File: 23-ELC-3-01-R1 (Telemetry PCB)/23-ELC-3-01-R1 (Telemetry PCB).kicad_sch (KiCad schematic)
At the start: 27 parts, among them J1 Conn_01x02, J10 Conn_02x12_Top_Bottom, J104 Raspberry_Pi_4b, J105 Conn_01x01, J106 Fan Header, J2 Conn_01x08, J4 Conn_01x02, J5 Conn_01x02, J7 Conn_01x08, J8 Conn_01x02

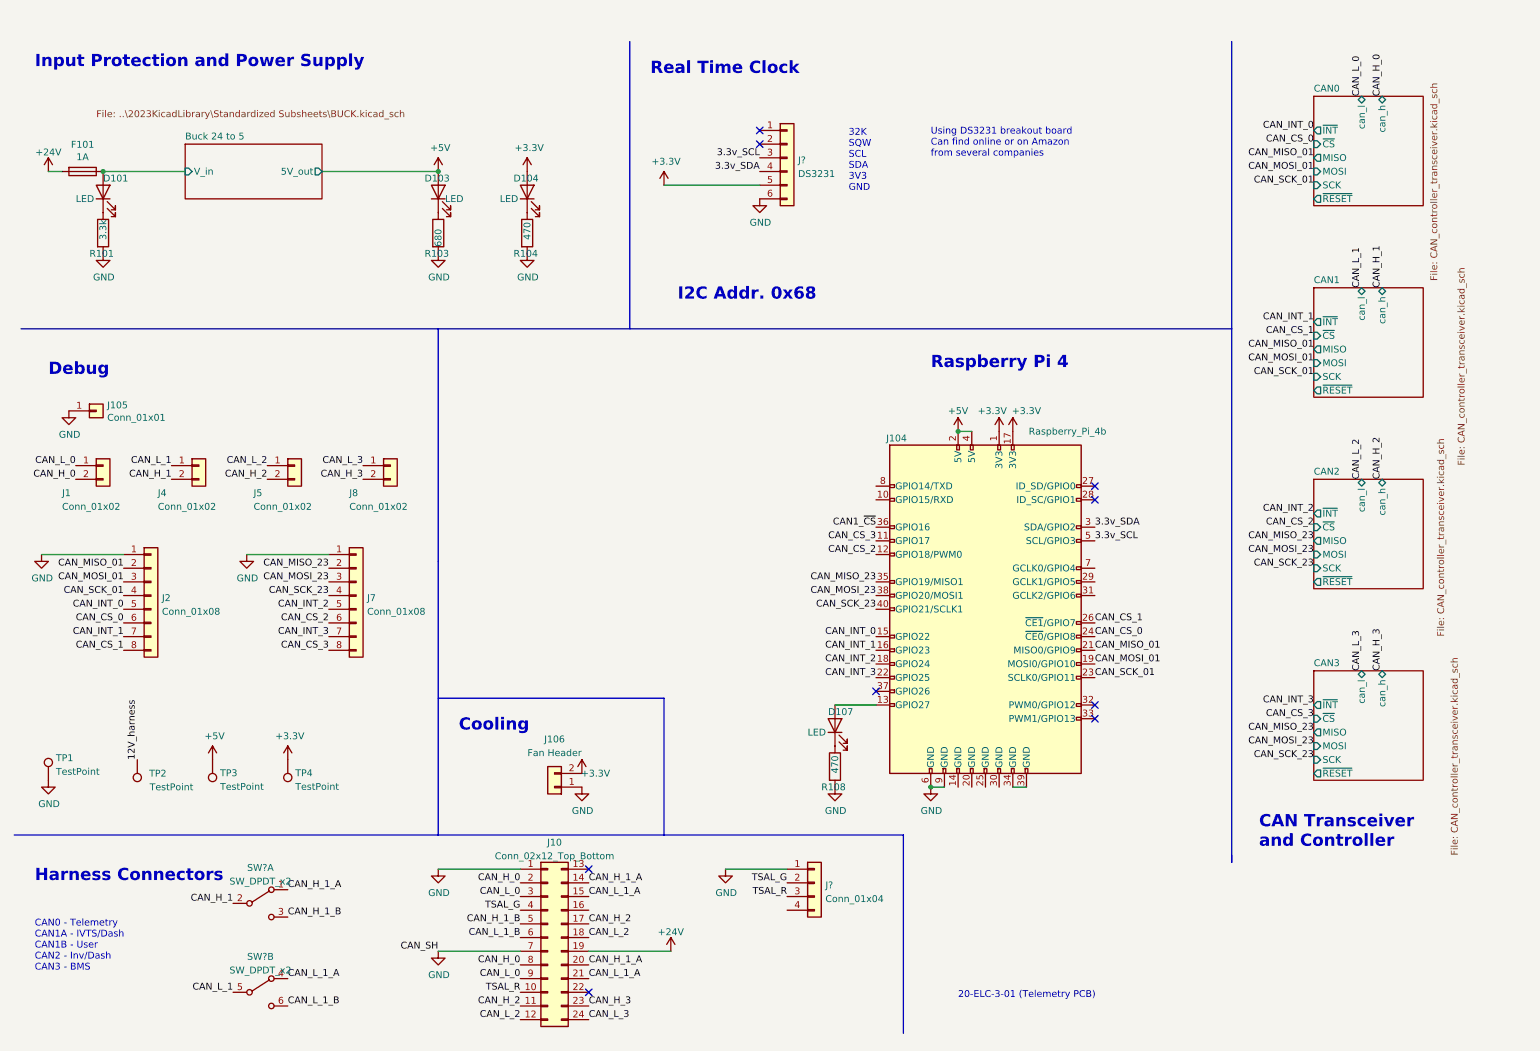
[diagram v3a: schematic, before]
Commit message: Schematic finished, working on layout
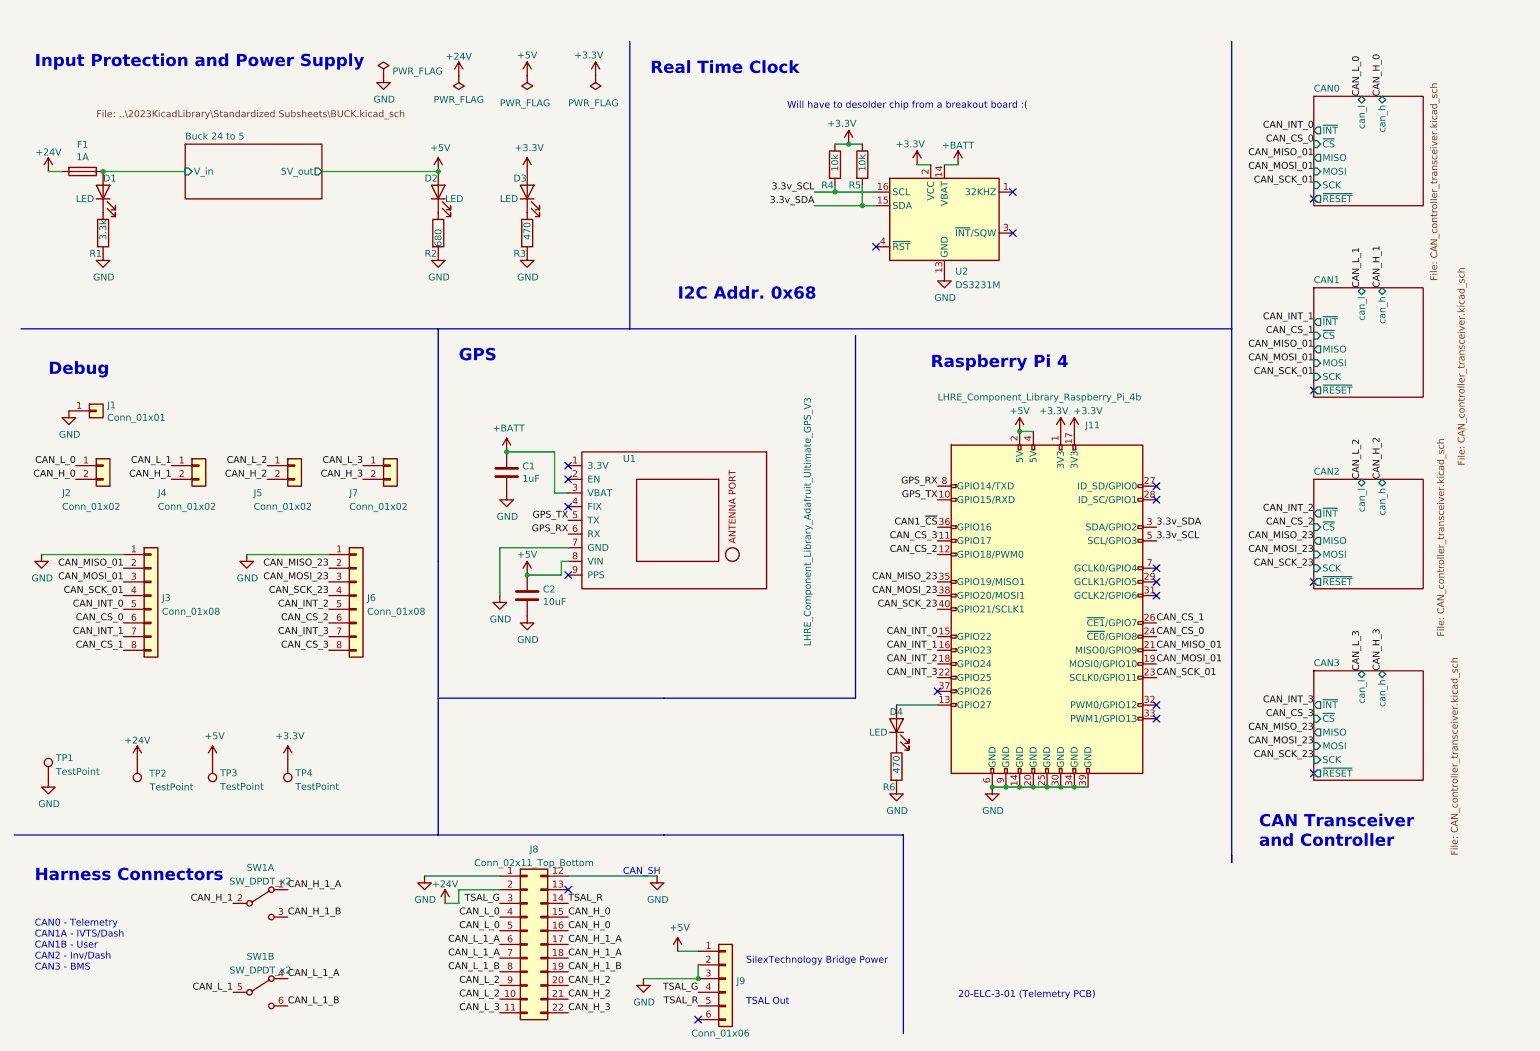
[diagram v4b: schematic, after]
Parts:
- removed D107: LED, LED_SMD:LED_0603_1608Metric_Pad1.05x0.95mm_HandSolder, symbol Device:LED
- removed J10: Conn_02x12_Top_Bottom, Global Libraries:DRC23-24PB, symbol Connector_Generic:Conn_02x12_Top_Bottom
- removed J104: Raspberry_Pi_4b, LHRE Footprint Library:Raspberry_Pi_4B_Socketed_THT_FaceDown_MountingHoles, symbol LHRE_Component_Library:Raspberry_Pi_4b
- removed J106: Fan Header, Connector_PinHeader_2.54mm:PinHeader_1x02_P2.54mm_Horizontal, symbol Connector_Generic:Conn_01x02
- removed J?: DS3231, Connector_PinHeader_2.54mm:PinHeader_1x06_P2.54mm_Vertical, symbol Connector_Generic:Conn_01x06
- removed J?: Conn_01x04, Connector_Molex:Molex_Micro-Fit_3.0_43045-0400_2x02_P3.00mm_Horizontal, symbol Connector_Generic:Conn_01x04
- removed R108: 470, Resistor_SMD:R_0603_1608Metric_Pad1.05x0.95mm_HandSolder, symbol Device:R
- added C1: 1uF, Capacitor_SMD:C_0805_2012Metric_Pad1.18x1.45mm_HandSolder, symbol Device:C
- added C2: 10uF, Capacitor_SMD:C_0805_2012Metric_Pad1.18x1.45mm_HandSolder, symbol Device:C
- added D4: LED, LED_SMD:LED_0603_1608Metric_Pad1.05x0.95mm_HandSolder, symbol Device:LED
- added J11: LHRE_Component_Library_Raspberry_Pi_4b, Global Libraries:Raspberry_Pi_4B_Socketed_THT_FaceDown_MountingHoles, symbol Global_Library:LHRE_Component_Library_Raspberry_Pi_4b
- added J8: Conn_02x11_Top_Bottom, Connector_Molex:Molex_Micro-Fit_3.0_43045-2200_2x11_P3.00mm_Horizontal, symbol Connector_Generic:Conn_02x11_Top_Bottom
- added J9: Conn_01x06, Connector_Molex:Molex_Micro-Fit_3.0_43045-0600_2x03_P3.00mm_Horizontal, symbol Connector_Generic:Conn_01x06
- added R4, R5: 10k, Resistor_SMD:R_0603_1608Metric_Pad0.98x0.95mm_HandSolder, symbol Device:R
- added R6: 470, Resistor_SMD:R_0603_1608Metric_Pad0.98x0.95mm_HandSolder, symbol Device:R
- added U1: LHRE_Component_Library_Adafruit_Ultimate_GPS_V3, Global Libraries:Adafruit_Ultimate_GPS_V3, symbol Global_Library:LHRE_Component_Library_Adafruit_Ultimate_GPS_V3
- added U2: DS3231M, Package_SO:SOIC-16W_7.5x10.3mm_P1.27mm, symbol Timer_RTC:DS3231M
- J3: renamed from J2; footprint (none) -> Connector_PinHeader_2.54mm:PinHeader_1x08_P2.54mm_Vertical
- J6: renamed from J7; footprint (none) -> Connector_PinHeader_2.54mm:PinHeader_1x08_P2.54mm_Vertical
- R1: renamed from R101; footprint Resistor_SMD:R_0603_1608Metric_Pad1.05x0.95mm_HandSolder -> Resistor_SMD:R_0603_1608Metric_Pad0.98x0.95mm_HandSolder
- R2: renamed from R103; footprint Resistor_SMD:R_0603_1608Metric_Pad1.05x0.95mm_HandSolder -> Resistor_SMD:R_0603_1608Metric_Pad0.98x0.95mm_HandSolder
- R3: renamed from R104; footprint Resistor_SMD:R_0603_1608Metric_Pad1.05x0.95mm_HandSolder -> Resistor_SMD:R_0603_1608Metric_Pad0.98x0.95mm_HandSolder
- SW1: renamed from SW?; footprint (none) -> Button_Switch_THT:SW_CuK_JS202011CQN_DPDT_Straight
- SW1: renamed from SW?; footprint (none) -> Button_Switch_THT:SW_CuK_JS202011CQN_DPDT_Straight; Part Number (none) -> JS202011CQN
- renumbered D101 to D1, D103 to D2, D104 to D3, F101 to F1, J105 to J1, J1 to J2, J8 to J7
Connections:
- net 12V_harness is gone; now on net +24V: TP2.1
- net +24V: now also J8.2 (Pin_2)
- net +3V3: now also J11.1 (3V3), J11.17 (3V3), R4.1, R5.1, U2.2 (VCC)
- net +5V: now also C2.1, J11.2 (5V), J11.4 (5V), J9.1 (Pin_1), U1.8 (VIN)
- net 3.3v_SCL: now also J11.5 (SCL/GPIO3), R4.2, U2.16 (SCL)
- net 3.3v_SDA: now also J11.3 (SDA/GPIO2), R5.2, U2.15 (SDA)
- net CAN1_~{CS}: now also J11.36 (GPIO16)
- net CAN_CS_0: now also J11.24 (~{CE0}/GPIO8)
- net CAN_CS_1: now also J11.26 (~{CE1}/GPIO7)
- net CAN_CS_2: now also J11.12 (GPIO18/PWM0)
- net CAN_CS_3: now also J11.11 (GPIO17)
- net CAN_H_0: now also J8.15 (Pin_15), J8.16 (Pin_16)
- net CAN_H_1_A: now also J8.17 (Pin_17), J8.18 (Pin_18)
- net CAN_H_1_B: now also J8.19 (Pin_19)
- net CAN_H_2: now also J8.20 (Pin_20), J8.21 (Pin_21)
- net CAN_H_3: now also J8.22 (Pin_22)
- net CAN_INT_0: now also J11.15 (GPIO22)
- net CAN_INT_1: now also J11.16 (GPIO23)
- net CAN_INT_2: now also J11.18 (GPIO24)
- net CAN_INT_3: now also J11.22 (GPIO25)
- net CAN_L_0: now also J8.4 (Pin_4), J8.5 (Pin_5)
- net CAN_L_1_A: now also J8.6 (Pin_6), J8.7 (Pin_7)
- net CAN_L_1_B: now also J8.8 (Pin_8)
- net CAN_L_2: now also J8.10 (Pin_10), J8.9 (Pin_9)
- net CAN_L_3: now also J8.11 (Pin_11)
- net CAN_MISO_01: now also J11.21 (MISO0/GPIO9)
- net CAN_MISO_23: now also J11.35 (GPIO19/MISO1)
- net CAN_MOSI_01: now also J11.19 (MOSI0/GPIO10)
- net CAN_MOSI_23: now also J11.38 (GPIO20/MOSI1)
- net CAN_SCK_01: now also J11.23 (SCLK0/GPIO11)
- net CAN_SCK_23: now also J11.40 (GPIO21/SCLK1)
- net GND: now also C1.2, C2.2, J11.14 (GND), J11.20 (GND), J11.25 (GND), J11.30 (GND), J11.34 (GND), J11.39 (GND), J11.6 (GND), J11.9 (GND), J8.1 (Pin_1), J8.12 (Pin_12), J9.2 (Pin_2), J9.3 (Pin_3), R6.2, U1.7 (GND), U2.10 (GND), U2.11 (GND), U2.12 (GND), U2.13 (GND), U2.5 (GND), U2.6 (GND), U2.7 (GND), U2.8 (GND), U2.9 (GND)
- net TSAL_G: now also J8.3 (Pin_3), J9.4 (Pin_4)
- net TSAL_R: now also J8.14 (Pin_14), J9.5 (Pin_5)
- new net: D4.2 (A), J11.13 (GPIO27)
- new net: D4.1 (K), R6.1
- new net +BATT: C1.1, U1.3 (VBAT), U2.14 (VBAT)
- new net GPS_RX: J11.8 (GPIO14/TXD), U1.6 (RX)
- new net GPS_TX: J11.10 (GPIO15/RXD), U1.5 (TX)
- no-connect marks 9 -> 21
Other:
- note added: "CAN_SH"
- note added: "GPS"
- note added: "SilexTechnology Bridge Power"
- note added: "TSAL Out"
- note added: "Will have to desolder chip from a breakout board :("
- note removed: "32K SQW SCL SDA 3V3 GND"
- note removed: "Cooling"
- note removed: "Using DS3231 breakout board Can find online or on Amazon from several companies"

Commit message: First draft of layout
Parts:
- removed J2, J4, J5, J7: Conn_01x02, Connector_PinHeader_2.54mm:PinHeader_1x02_P2.54mm_Vertical, symbol Connector_Generic:Conn_01x02
- added C29, C30: 1uF, Capacitor_SMD:C_0805_2012Metric_Pad1.18x1.45mm_HandSolder, symbol Device:C
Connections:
- net +3V3: now also C29.1
- net +BATT: now also C30.1
- net GND: now also C29.2, C30.2
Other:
- note added: "Decoupling"
